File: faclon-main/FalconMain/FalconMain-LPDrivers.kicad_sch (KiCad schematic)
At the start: 0 parts

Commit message: Reorganize
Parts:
- added C29, C36: 100nF, Capacitor_SMD:C_0402_1005Metric, symbol Device:C_Small
- added C30: 12pF, Capacitor_SMD:C_0402_1005Metric, symbol Device:C_Small
- added C31, C32, C35, C39: 10uF, Capacitor_SMD:C_1210_3225Metric, symbol Device:C_Small
- added C33, C34: 1uF, Capacitor_SMD:C_0603_1608Metric, symbol Device:C_Small
- added C37: 10nF, Capacitor_SMD:C_0402_1005Metric, symbol Device:C_Small
- added C38: 510pF, Capacitor_SMD:C_0402_1005Metric, symbol Device:C_Small
- added D2, D3: 500mA, JetkovKiCADLib:SC-76-SOD-323_USC_TSB, symbol Device:D_Schottky_Small
- added D4: 20A, JetkovKiCADLib:TO-252-2-3_DPAK_ST, symbol JetkovKiCADLib:D_Schottky_AAK_Small
- added L3: 10uH, Inductor_SMD:L_1008_2520Metric, symbol Device:L_Small
- added L4: 47uH, JetkovKiCADLib:AMDLA1306S, symbol Device:L_Small
- added Q17: Q_PMOS_LFPAK, JetkovKiCADLib:LFPACK56-S08_SOT669_NXP, symbol JetkovKiCADLib:Q_PMOS_LFPAK
- added Q18: Q_PMOS_GSD, JetkovKiCADLib:SC-96_TSMT3_ROM, symbol Device:Q_PMOS_GSD
- added Q19, Q20, Q21: Q_NMOS_GSD, JetkovKiCADLib:SOT-323_SC-70, symbol Device:Q_NMOS_GSD
- added R41: 442k, Resistor_SMD:R_0402_1005Metric, symbol Device:R_Small
- added R42: 402k, Resistor_SMD:R_0402_1005Metric, symbol Device:R_Small
- added R43, R44, R46, R49, R54, R57: 100k, Resistor_SMD:R_0402_1005Metric, symbol Device:R_Small
- added R45: 49.9k, Resistor_SMD:R_0402_1005Metric, symbol Device:R_Small
- added R47: 44.2k, Resistor_SMD:R_0402_1005Metric, symbol Device:R_Small
- added R48, R52, R56: 2k, Resistor_SMD:R_0402_1005Metric, symbol Device:R_Small
- added R50: 0R, Resistor_SMD:R_0402_1005Metric, symbol Device:R_Small
- added R51: DNP, Resistor_SMD:R_0402_1005Metric, symbol Device:R_Small
- added R53: 39m, Resistor_SMD:R_1206_3216Metric, symbol Device:R_Small
- added R55: 1M, Resistor_SMD:R_0402_1005Metric, symbol Device:R_Small
- added U4: BD9E104FJ-E2, JetkovKiCADLib:8-SOIC_8-SOP-J_ROHM, symbol JetkovKiCADLib:BD9E104FJ-E2
- added U5: NCP164ASN330T1G, JetkovKiCADLib:SOT-23-5_TSOP−5_ON, symbol JetkovKiCADLib:NCP164ASN330T1G
- added U6: AL8843QSP-13, JetkovKiCADLib:8-SOIC_SO-8EP_DIO, symbol JetkovKiCADLib:AL8843QSP-13
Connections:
- new net: C37.2, Q17.4 (G), Q18.1 (G), R46.2
- new net: Q19.3 (D), R48.2
- new net: C29.1, U4.1 (BOOT)
- new net: D3.1 (K), R41.1, R43.2, U4.3 (EN)
- new net: C30.2, R42.2, R44.2, U4.5 (FB)
- new net: C38.1, U4.6 (COMP)
- new net: C29.2, L3.1, U4.8 (SW)
- new net: D4.1 (A), D4.2 (A), L4.1, U6.7 (SW), U6.8 (SW)
- new net: D2.1 (K), R41.2
- new net: C38.2, R47.1
- new net: R45.2, R46.1, R48.1
- new net +19V5: D2.2 (A)
- new net +3V3: C34.2, U5.5 (OUT)
- new net +4V: C30.1, C31.2, C32.2, C33.2, L3.2, Q18.2 (S), R42.1, U5.1 (IN), U5.3 (EN)
- new net +4V_SW: Q18.3 (D)
- new net +5V1: R50.2
- new net DRV_PIEZO_LHS: Q20.3 (D), R52.1
- new net DRV_PIEZO_RHS: Q21.3 (D), R56.1
- new net EN_4V: D3.2 (A)
- new net EN_HIGH_POWER: Q19.1 (G), R49.2
- new net FRONT_LED_N: L4.2
- new net FRONT_LED_P: R53.1, U6.3 (SET)
- new net GND: C31.1, C32.1, C33.1, C34.1, C35.1, C36.1, C39.1, Q19.2 (S), Q20.2 (S), Q21.2 (S), R43.1, R44.1, R47.2, R49.1, R54.1, R55.1, R57.1, U4.4 (GND), U4.7 (PGND), U5.2 (GND), U6.1 (GND), U6.2 (GND), U6.EPAD
- new net PWM_LED_FRONT: R55.2, U6.5 (CTRL)
- new net PWM_PIEZO_LHS: Q20.1 (G), R54.2
- new net PWM_PIEZO_RHS: Q21.1 (G), R57.2
- new net VBAT: R51.2
- new net VPIEZO: R50.1, R51.1, R52.2, R56.2
- new net VSYS: C35.2, C36.2, C37.1, Q17.1 (S), Q17.2 (S), Q17.3 (S), R45.1, U4.2 (VIN)
- new net VSYS_SW: C39.2, D4.3 (K), Q17.5 (D), R53.2, U6.6 (VIN)
- no-connect marks 0 -> 1
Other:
- note added: "12-14pF"
- note added: "12-19.5V/0.7A to 4V/0.2A Buck Regulator"
- note added: "170mV dropout @ 3.3V/300mA ±2% Accuracy"
- note added: "19.5V supply enables power to the MCU. MCU should maintain 4V_EN high"
- note added: "4A"
- note added: "4V to 3.3V LDO"
- note added: "Alt: C_{OUT}=30uF, R_{4}=64.9kOhms, C_{4}=360pF"
- note added: "Check Min On-Time Spec -------------------- 250ns<=1.75(V_{OUT}/V_{IN}) 250ns<=1.75(4/19)=368ms"
- note added: "Could place zener across capacitor to ensure fixed clamp voltage"
- note added: "Enable 4V_SW with VSYS_SW to power the 5.1V buck regulator LV circuits"
- note added: "Front LED Driver"
- note added: "HIGH POWER SWITCH"
- note added: "Heatsink"
- note added: "I_{Q}=250uA I_{off}=10uA P_{off}=148uW"
- note added: "I_{off}=?"
- note added: "I_{out}=0.1V/R_{set} R_{set}=0.1V/2.5A ~=0.039R"
- note added: "I_{q}=350uA CTRL floating"
- note added: "LOW POWER 4V AND 3.3V REGULATION"
- note added: "LV PMOS will turn on after HV, and turn off before HV"
- note added: "Loop Compensation ------------------------ R_{4}=[(2pi)(V_{OUT})(f_{CRS})(C_{OUT})]/[(V_{FB})(G_{MP})(G_{MA})] =[(2pi)(V_{OUT})(f_{CRS})(C_{OUT})]/[(0.8V)(7A/V)(82uA/V)] =13682.8948(V_{OUT})(f_{CRS})(C_{OUT}) =13682.8948(4)(40e3)(20e-6) =43.785kOhms~=44.2kOhms C_{4}=1/[(2pi)(R_{4})(f_{CRS}/6)] =1/[(2pi)(44.2e3)(40e3/6)] =540pF~=510pF"
- note added: "Maximum Load Capacitance ----------------- C_{LOAD-MAX}=[(t_{ss})(I_{LIM}-I_{OUTMAX}-I_{RPL}/2)/V_{OUT}]-C_{OUT} =[(1.2e-3)(2.1-0.2-0.526/2)/4]-20e-6 =471uF"
- note added: "ON-BOARD LOAD DRIVERS"
- note added: "Output Voltage Set ------------------------ V_{OUT}=0.8[(R_{1}+R_{2})/R_{2}] =0.8*[(402+100)/100]=4.016V"
- note added: "Piezo Drivers"
- note added: "RHS"
- note added: "Ripple Current at Selected Inductance ------------------------ I_{RPL}=(V_{OUT})(V_{IN}-V_{OUT})/[(V_{IN})(f_{OSC})(L)] =(4V)(16V-4V)/[(16V)(570kHz)(10uH)] =0.526A Ripple Voltage at Selected Output Capacitance ------------------------ V_{RPL}=I_{RPL}[R_{ESR}+1/(8(C_{OUT})(f_{OSC}))] =(0.526A)[0.005Ohm+1/(8(20uF)(570kHz))] =8.40mV"
- note added: "V_{TL}=0.8V V_{TH}=2.5V"
- note added: "f_{OSC}=570kHz f_{CRS}=40kHz"
- note added: "t_{ON(MIN)}=500nS"
- note added: "t_{ON}=[L(0.26)(I_{LED})]/[V_{IN}-V_{LED}-I_{LED}(R_{SET}+R_{L}+R_{SW})] =[47uH(0.26)(3A)]/[14.8V-3V-3A(0.039+0.1+0.2)Ohms] =3.3997uS"

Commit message: Layout WIP
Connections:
- net VBAT is gone; now on net VSYS: R51.2
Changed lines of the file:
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@@
+    (pin "1")
+  )
+  (symbol (lib_id "JetkovKiCADLib:VSYS") (at 46.99 129.54 0) (unit 1)
+    (in_bom yes) (on_board yes) (fields_autoplaced)
+    (property "Reference" "#PWR0104" (id 0) (at 46.99 133.35 0)
+      (effects (font (size 1.27 1.27)) hide)
+    )
+    (property "Value" "VSYS" (id 1) (at 46.99 125.73 0))
+    (property "Footprint" "" (id 2) (at 46.99 129.54 0)
+      (effects (font (size 1.27 1.27)) hide)
+    )
+    (property "Datasheet" "" (id 3) (at 46.99 129.54 0)
+      (effects (font (size 1.27 1.27)) hide)
+    )
     (pin "1")
   )
@@
       (effects (font (size 1.27 1.27)) hide)
     )
-    (pin "1")
-  )
-  (symbol (lib_id "JetkovKiCADLib:VBAT") (at 46.99 129.54 0) (unit 1)
-    (in_bom yes) (on_board yes) (fields_autoplaced)
-    (property "Reference" "#PWR0104" (id 0) (at 46.99 133.35 0)
-      (effects (font (size 1.27 1.27)) hide)
-    )
-    (property "Value" "VBAT" (id 1) (at 46.99 125.73 0))
-    (property "Footprint" "" (id 2) (at 46.99 129.54 0)
-      (effects (font (size 1.27 1.27)) hide)
-    )
-    (property "Datasheet" "" (id 3) (at 46.99 129.54 0)
-      (effects (font (size 1.27 1.27)) hide)
-    )

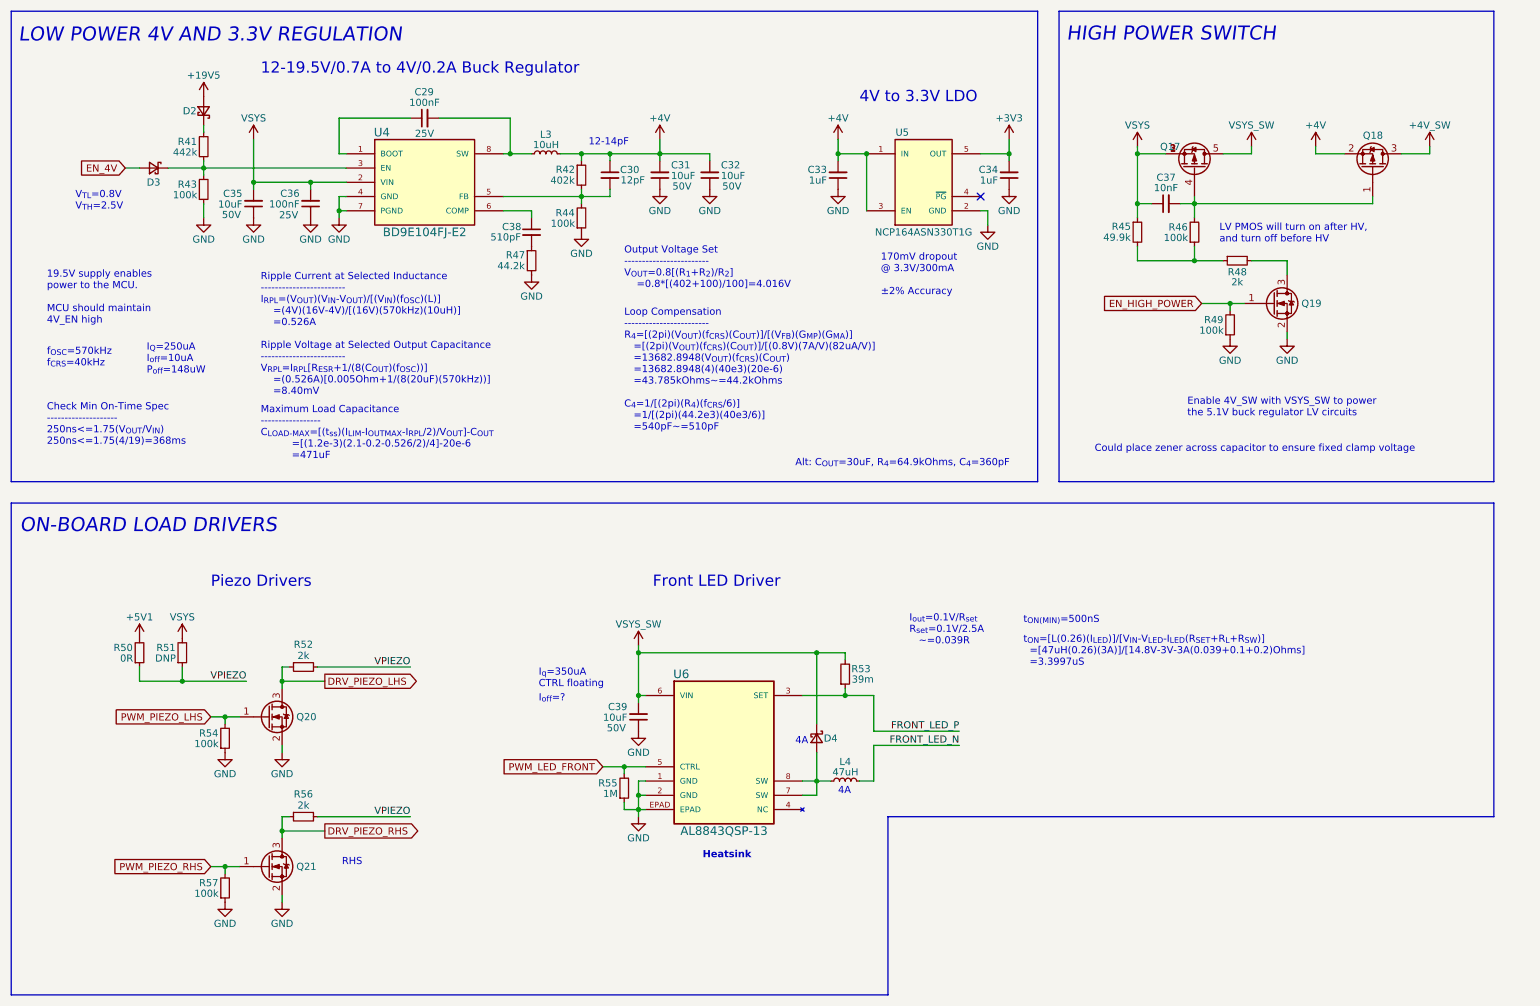
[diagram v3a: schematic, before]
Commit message: Large component rough placement
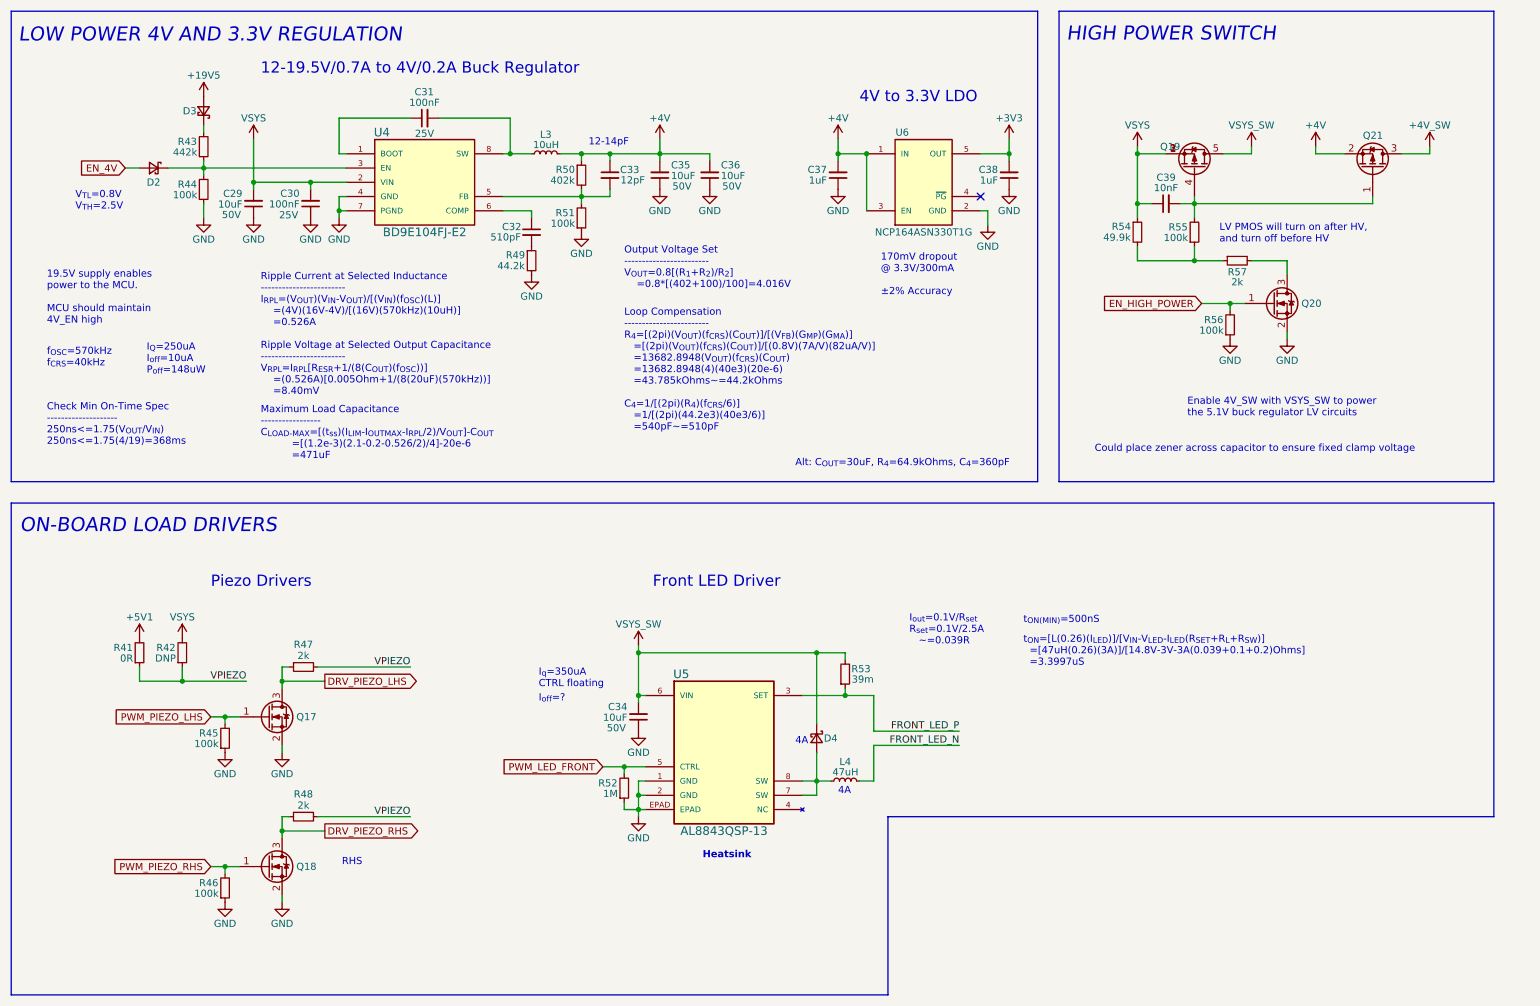
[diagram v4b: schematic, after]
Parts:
- renumbered C35 to C29, C36 to C30, C29 to C31, C38 to C32, C30 to C33, C39 to C34, C31 to C35, C32 to C36, C33 to C37, C34 to C38, C37 to C39, D3 to D2, D2 to D3, Q20 to Q17, Q21 to Q18, Q17 to Q19, Q19 to Q20, Q18 to Q21, R50 to R41, R51 to R42, R41 to R43, R43 to R44, R54 to R45, R57 to R46, R52 to R47, R56 to R48, R47 to R49, R42 to R50, R44 to R51, R55 to R52, R45 to R54, R46 to R55, R49 to R56, R48 to R57, U6 to U5, U5 to U6

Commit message: Rought placement done
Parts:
- renumbered C29 to C31, C30 to C32, C31 to C33, C32 to C34, C33 to C35, C34 to C36, C35 to C37, C36 to C38, C37 to C39, C38 to C40, C39 to C41
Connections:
- net VSYS: no longer R42.2
- net ~{EN_HIGH_POWER}: now reaches C41.2, Q19.4 (G), Q21.1 (G), R55.2
- new net VSYS_SW_FUSED: R42.2

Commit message: Reviewed again
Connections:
- net 4VB_BOOT: now reaches C33.1, U4.1 (BOOT)
- net 4VB_EN: now reaches D2.1 (K), R43.1, R44.2, U4.3 (EN)
- net 4VB_FB: now reaches C35.2, R50.2, R51.2, U4.5 (FB)
- net 4VB_CMP: now reaches C34.1, U4.6 (COMP)
- net 4VB_SW: now reaches C33.2, L3.1, U4.8 (SW)
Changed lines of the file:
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@@
     (effects (font (size 1.27 1.27)) (justify right bottom))
+  )
+  (label "4VB_BOOT" (at 78.74 36.83 0)
+    (effects (font (size 0.8 0.8)) (justify left bottom))
   )
   (label "FRONT_LED_N" (at 185.42 148.59 180)
     (effects (font (size 1.27 1.27)) (justify right bottom))
   )
+  (label "4VB_EN" (at 69.85 45.72 0)
+    (effects (font (size 0.8 0.8)) (justify left bottom))
+  )
+  (label "4VB_CMP" (at 104.14 53.34 0)
+    (effects (font (size 0.8 0.8)) (justify left bottom))
+  )
   (label "VPIEZO" (at 87.63 134.62 180)
     (effects (font (size 1.27 1.27)) (justify right bottom))
   )
+  (label "4VB_FB" (at 104.14 50.8 0)
+    (effects (font (size 0.8 0.8)) (justify left bottom))
+  )
+  (label "4VB_SW" (at 96.52 36.83 0)
+    (effects (font (size 0.8 0.8)) (justify left bottom))
+  )
   (label "~{EN_HIGH_POWER}" (at 238.76 52.07 0)

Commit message: Layour WIP
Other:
- note removed: "RHS"
- moved on the sheet: Q17, Q18, R41, R45, R46, R47, R48
